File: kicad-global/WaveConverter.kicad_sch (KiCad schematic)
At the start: 27 parts, among them J7 Sine, J8 Tri, U3 LM13700, U4 TL074

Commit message: update components
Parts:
- Sine_Bias_trim, Sine_Lvl_trim, Sine_Shape_trim: Comments (none) -> Use multi turn Cermet style 3296 pots
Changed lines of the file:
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@@
+      (effects (font (size 1.27 1.27)) hide)
+    )
+    (property "manf" "" (at 100.33 110.49 90)
+      (effects (font (size 1.27 1.27)) hide)
+    )
+    (property "manf#" "" (at 100.33 110.49 90)
+      (effects (font (size 1.27 1.27)) hide)
+    )
+    (property "Comments" "Use multi turn Cermet style 3296 pots " (at 100.33 110.49 90)
       (effects (font (size 1.27 1.27)) hide)
     )
@@
     )
   )
-  (symbol (lib_id "Device:R_POT") (at 67.31 101.6 270) (unit 1)
-    (in_bom yes) (on_board yes) (dnp no)
-    (property "Reference" "Sine_Shape_trim" (at 67.31 97.79 90)
-      (effects (font (size 1.27 1.27)))
-    )
-    (property "Value" "100k" (at 69.85 101.6 90)
-      (effects (font (size 1.27 1.27)) (justify right))
-    )
-    (property "Footprint" "Potentiometer_THT:Potentiometer_Bourns_3386C_Horizontal" (at 67.31 101.6 0)
-      (effects (font (size 1.27 1.27)) hide)
-    )
-    (property "Datasheet" "~" (at 67.31 101.6 0)
-      (effects (font (size 1.27 1.27)) hide)
-    )
-    (pin "1")
-    (pin "2")
-    (pin "3")
-    (instances
-      (project "CD40106_VCO"
-        (path "/fea7c5d1-76d6-41a0-b5e3-29889dbb8ce0/9c69c853-342d-4663-b733-f98569aee5a3"
-          (reference "Sine_Shape_trim") (unit 1)
-        )
-      )
-    )
-  )
   (symbol (lib_id "Amplifier_Operational:TL074") (at 93.98 31.75 0) (unit 1)
     (in_bom yes) (on_board yes) (dnp no)
@@
     )
   )
+  (symbol (lib_id "Device:R_POT") (at 67.31 101.6 270) (unit 1)
+    (in_bom yes) (on_board yes) (dnp no)
+    (property "Reference" "Sine_Shape_trim" (at 67.31 97.79 90)
+      (effects (font (size 1.27 1.27)))
+    )
+    (property "Value" "100k" (at 69.85 101.6 90)
+      (effects (font (size 1.27 1.27)) (justify right))
+    )
+    (property "Footprint" "Potentiometer_THT:Potentiometer_Bourns_3386C_Horizontal" (at 67.31 101.6 0)
+      (effects (font (size 1.27 1.27)) hide)
+    )
+    (property "Datasheet" "~" (at 67.31 101.6 0)
+      (effects (font (size 1.27 1.27)) hide)
+    )
+    (property "manf" "" (at 67.31 101.6 90)
+      (effects (font (size 1.27 1.27)) hide)
+    )
+    (property "manf#" "" (at 67.31 101.6 90)
+      (effects (font (size 1.27 1.27)) hide)
+    )
+    (property "Comments" "Use multi turn Cermet style 3296 pots " (at 67.31 101.6 90)
+      (effects (font (size 1.27 1.27)) hide)
+    )
+    (pin "1")
+    (pin "2")
+    (pin "3")
+    (instances
+      (project "CD40106_VCO"
+        (path "/fea7c5d1-76d6-41a0-b5e3-29889dbb8ce0/9c69c853-342d-4663-b733-f98569aee5a3"
+          (reference "Sine_Shape_trim") (unit 1)
+        )
+      )
+    )
+  )
   (symbol (lib_id "Device:R") (at 139.7 121.92 270) (unit 1)
     (in_bom yes) (on_board yes) (dnp no)
@@
       (effects (font (size 1.27 1.27)) hide)
     )
+    (property "manf" "" (at 40.64 105.41 90)
+      (effects (font (size 1.27 1.27)) hide)
+    )
+    (property "manf#" "" (at 40.64 105.41 90)
+      (effects (font (size 1.27 1.27)) hide)
+    )
+    (property "Comments" "Use multi turn Cermet style 3296 pots " (at 40.64 105.41 90)
+      (effects (font (size 1.27 1.27)) hide)
+    )

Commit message: finished v1 of module
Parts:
- removed J7: Sine, Synth:Thonkiconn, symbol Connector:AudioJack2_SwitchT
- removed J8: Tri, Synth:Thonkiconn, symbol Connector:AudioJack2_SwitchT
- added J13: Sine, Kicad-perso:Thonkiconn, symbol Kicad-perso:AudioJack_Switch
- added J14: Conn_01x02, Connector_PinHeader_2.54mm:PinHeader_1x02_P2.54mm_Vertical, symbol Connector_Generic:Conn_01x02
- added J15: Tri, Kicad-perso:Thonkiconn, symbol Kicad-perso:AudioJack_Switch
- C8: renamed from C13; value 1u -> 1uF
- C9: renamed from C14; value 1u -> 1uF
- Sine_Bias_trim1: renamed from Sine_Bias_trim; manf (none) -> ALPHA
- Sine_Lvl_trim1: renamed from Sine_Lvl_trim; manf (none) -> ALPHA
- Sine_Shape_trim1: renamed from Sine_Shape_trim; manf (none) -> ALPHA
- U6: renamed from U3; manf (none) -> Texas Instrument; manf# (none) -> LM13700MX/NOPB
- renumbered R20 to R27, R21 to R28, R22 to R29, R23 to R30, R24 to R31, R25 to R32, R26 to R33, R27 to R34, R28 to R35, R29 to R36, R30 to R37, R31 to R38, R32 to R39, R33 to R40, R34 to R42, R35 to R44, U4 to U7
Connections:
- net GND: now also J13.S, J14.2 (Pin_2), J15.S
- net Saw: now also J14.1 (Pin_1)
- net Sine_out renamed Sine out
- net Sine out: now also J13.T
- net Tri_out renamed Tri out
- net Tri out: now also J15.T
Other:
- note added: "Connector to SubPhatty extendor"
- moved on the sheet: R27, R28, R29, R31, R32, R33, R35, R36, Sine_Bias_trim1, Sine_Lvl_trim1, Sine_Shape_trim1, U6A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

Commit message: doc + fab files for V1.0
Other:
- company: (none) -> Bleep Sound
- title: (none) -> CD40106 VCO
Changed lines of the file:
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@@
 (kicad_sch (version 20230121) (generator eeschema)
   (paper "A4")
+  (title_block
+    (title "CD40106 VCO")
+    (date "2023-12-10")
+    (rev "1.0")
+    (company "Bleep Sound")
+  )
   (junction (at 60.96 143.51) (diameter 0) (color 0 0 0 0)
   )

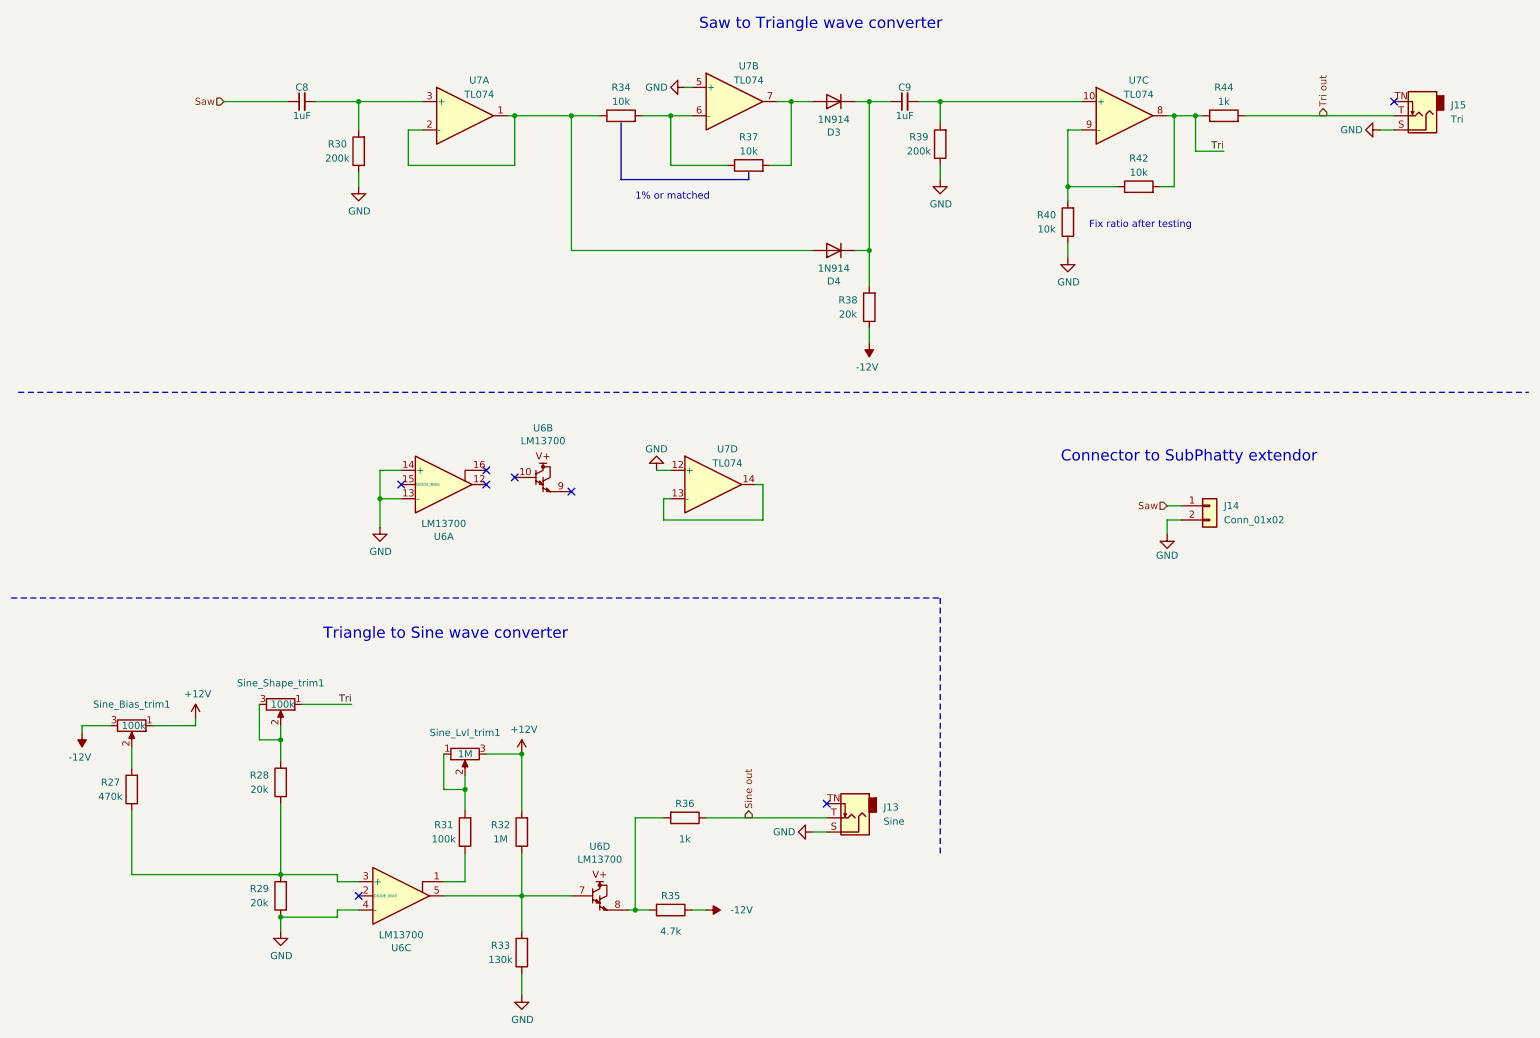
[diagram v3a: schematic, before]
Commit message: First proto fix
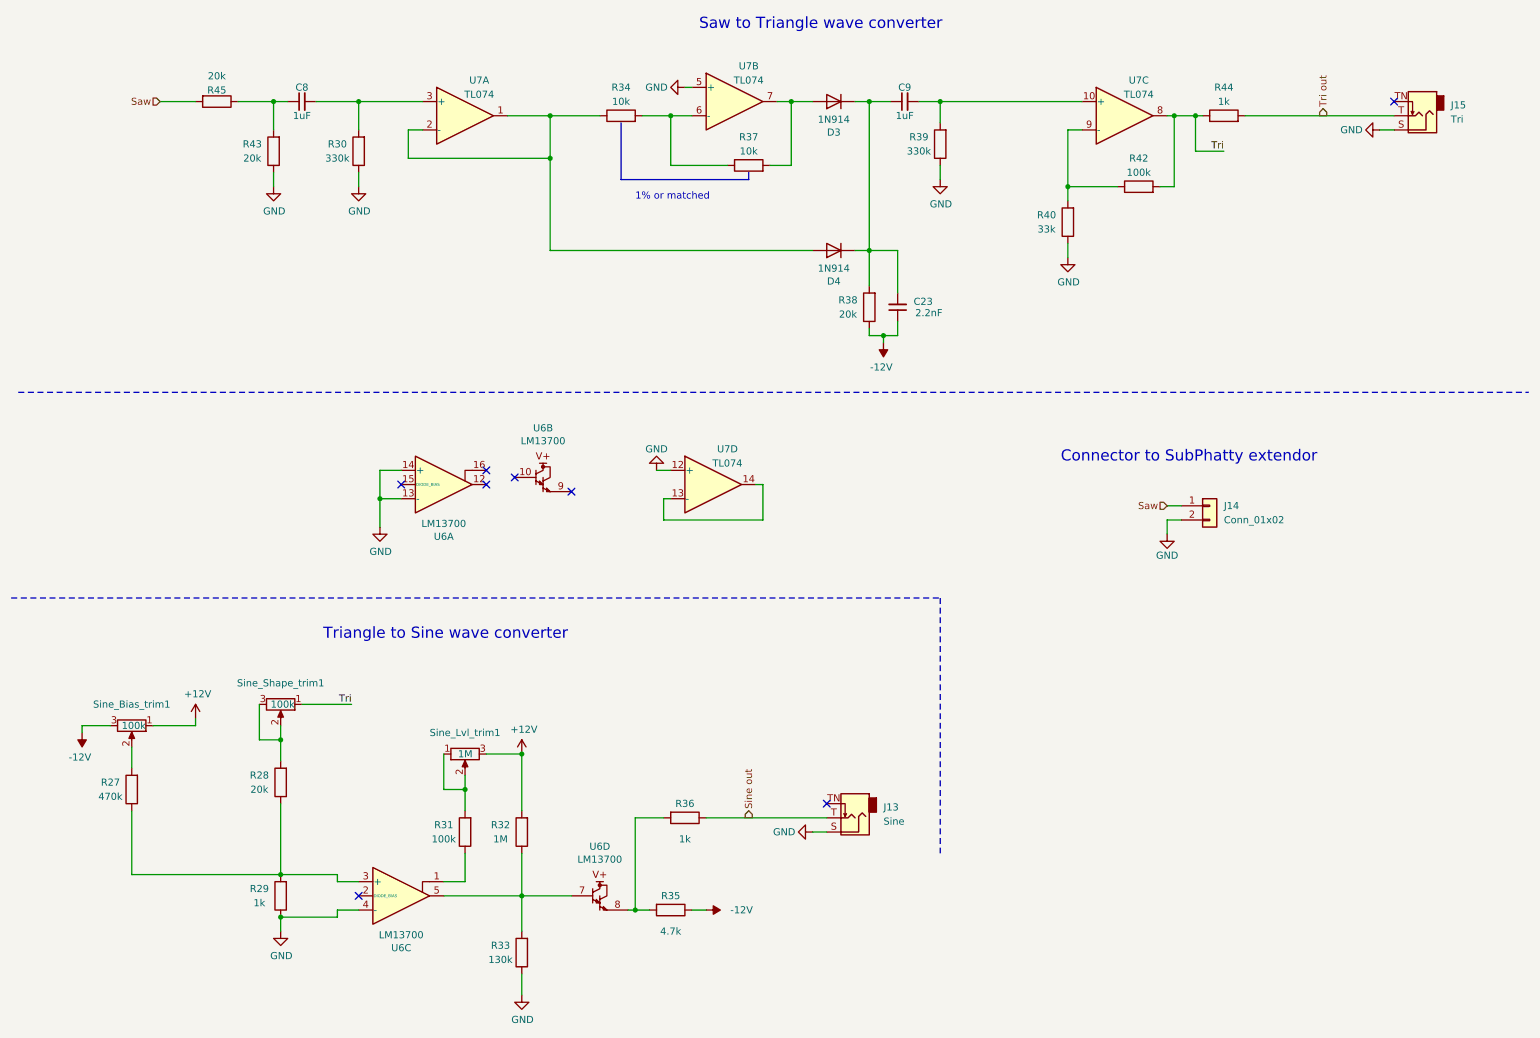
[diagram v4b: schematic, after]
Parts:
- added C23: 2.2nF, Capacitor_THT:C_Disc_D7.0mm_W2.5mm_P5.00mm, symbol Device:C_Small
- added R43, R45: 20k, Resistor_THT:R_Axial_DIN0207_L6.3mm_D2.5mm_P10.16mm_Horizontal, symbol Device:R
- R29: value 20k -> 1k
- R30, R39: value 200k -> 330k
- R40: value 10k -> 33k
- R42: value 10k -> 100k
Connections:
- net -12V: now also C23.1
- net GND: now also R43.1
- net Saw: now also R45.2; no longer C8.1
- net at C9.1, D3.1 (K), D4.1 (K)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: now also C23.2
- new net: C8.1, R43.2, R45.1
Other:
- note removed: "Fix ratio after testing"

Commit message: V2.0
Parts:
- C23, C8, C9: Links (none) -> https://www.taydaelectronics.com/capacitors/monolithic-cera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
- D3, D4: Links (none) -> https://www.taydaelectronics.com/1n914-small-signal-diode-2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
- J13, J15: Comments Thonkiconn jack -> (none); Links (none) -> https://www.thonk.co.uk/shop/thonkiconn/
- R27, R28, R29, R30, R31, R32, R33, R34, R35, R36, R37, R38, R39, R40, R42, R43, R44, R45: Links (none) -> https://www.taydaelectronics.com/resistors/1-4w-metal-film-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
- Sine_Bias_trim1, Sine_Shape_trim1: footprint Potentiometer_THT:Potentiometer_Bourns_3386C_Horizontal -> Potentiometer_THT:Potentiometer_Bourns_3296W_Vertical; Comments Use multi turn Cermet style 3296 pots -> (none); Links (none) -> Trimmer potentiometer, 25 turn series 3296W; manf ALPHA -> (none)
- Sine_Lvl_trim1: footprint Potentiometer_THT:Potentiometer_Bourns_3386C_Horizontal -> Potentiometer_THT:Potentiometer_Bourns_3296W_Vertical; Comments Use multi turn Cermet style 3296 pots -> (none); Links (none) -> https://www.thonk.co.uk/shop/25-turn-trimmer-potentiometer/; manf ALPHA -> (none)
- U6: Links (none) -> https://eu.mouser.com/c/semiconductors/amplifier-ics/transc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
- U7: Links (none) -> https://www.thonk.co.uk/shop/eurorack-diy-essentials/; manf (none) -> Texas Instrument; manf# (none) -> TL074CN
